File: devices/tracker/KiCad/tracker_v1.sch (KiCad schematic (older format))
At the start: 45 parts, among them J1 Conn_01x06_Male, J2 Conn_01x09_Male, Q1 AO3401A, U1 STM32L412KB, U2 RFM95W-868S2, U3 ublox_SAM-M8Q, U4 LIS3DH, Y1 32KHz

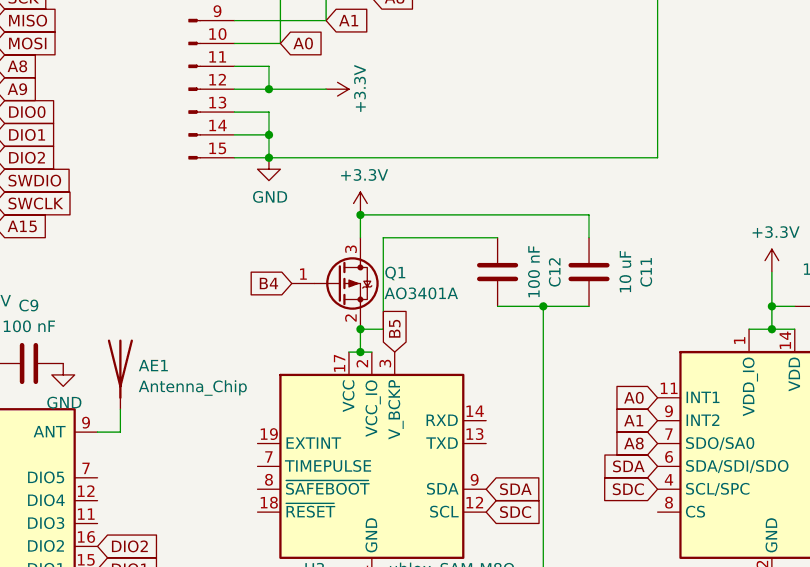
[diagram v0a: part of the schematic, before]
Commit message: Adding tracker - before class rework
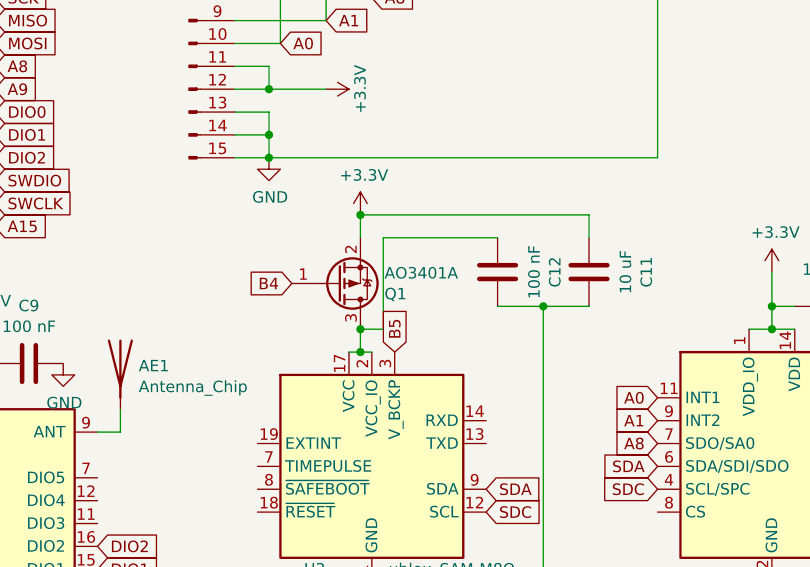
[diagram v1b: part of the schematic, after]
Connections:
- net +3V3: now also Q1.2 (S); no longer Q1.3 (D)
- net at C12.2, U3.17 (VCC), U3.2 (VCC_IO): now also Q1.3 (D); no longer Q1.2 (S)
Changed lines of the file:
@@
 F 3 "http://www.aosmd.com/pdfs/datasheet/AO3401A.pdf" H 8150 4100 50  0001 L CNN
 	1    8150 4100
-	1    0    0    -1
+	1    0    0    1
 $EndComp
 $Comp
